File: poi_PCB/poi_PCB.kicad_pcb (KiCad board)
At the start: 2 copper layers, 60 x 60 mm, 73 parts, among them J1 ANALOG_RGB_HEADER, J4 USB_C_Receptacle_USB2.0, Q1 AO4407C, Q2 AO3400A, Q3 AO3400A, Q4 AO3400A, Q5 AO4407C, Q6 AO3400A, Q7 AO3400A, Q8 AO3400A, SW3 TL2233OA, U1 ESP32-WROOM-32D, U2 CH340C, U3 AMS1117-3.3, U4 LSM6DS33TR, U5 LIS2DH, U6 MH-CD42

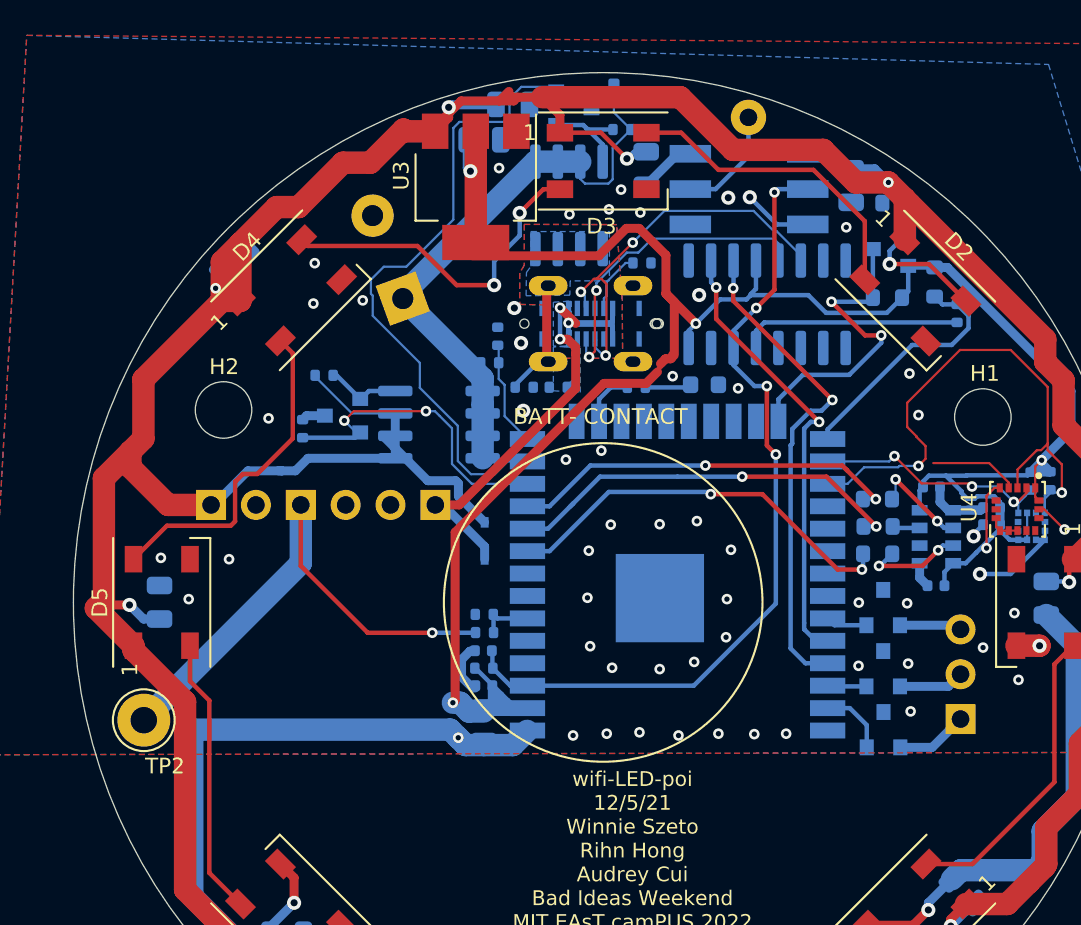
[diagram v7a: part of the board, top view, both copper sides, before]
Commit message: Changed schematic based on testing
-LED logic level shifter omitted due to slow switching speed of AO3400A
-LED input moved to GPIO5 to avoid pulling up GPIO2 during UART programming
-Gate pullup/pulldown resistors changed to 1K to allow for faster switching
-analog RGB header omitted
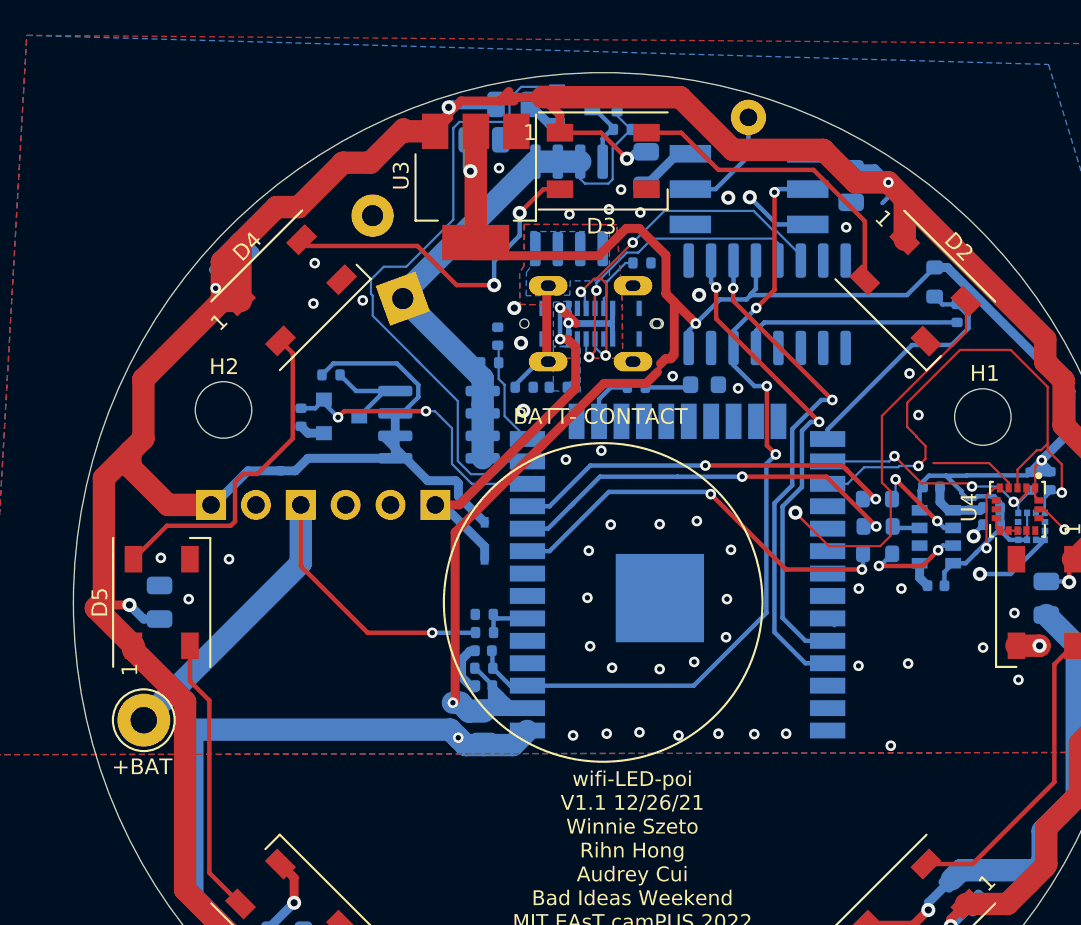
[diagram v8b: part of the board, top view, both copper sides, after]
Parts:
- removed J1: ANALOG_RGB_HEADER, Connector_PinHeader_2.54mm:PinHeader_1x03_P2.54mm_Vertical
- removed Q3, Q4, Q7, Q8: AO3400A, Package_TO_SOT_SMD:SOT-23
- removed R14, R15: 10K, Resistor_SMD:R_0603_1608Metric
- C4: value CP1_Small -> 0.47F
- R11, R13, R17, R18: value 10K -> 1K
- moved Q6 33.2 mm to (105.9, 49.5), turned to 0 degrees
- moved R13 0.65 mm to (90.4, 67.0), turned to 90 degrees
- moved R17 0.62 mm to (108.3, 49.2)
- moved R11 0.39 mm to (92.1, 64.6)
- moved Q2 0.07 mm to (92.7, 67.0), turned to 0 degrees
- renumbered TP2 to +BAT, TP1 to EN_L
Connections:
- D2 pad 4: /LED_SIG_5 -> /LED_SIG
- Q2 pad 1: Net-(Q1-Pad4) -> GND
- Q2 pad 3: GND -> Net-(Q1-Pad4)
- Q5 pad 4: Net-(Q4-Pad1) -> Net-(Q5-Pad4)
- Q6 pad 1: Net-(J1-Pad3) -> GND
- Q6 pad 2: /RED -> /FIRE_L
- Q6 pad 3: GND -> Net-(Q5-Pad4)
- R18 pad 2: Net-(Q4-Pad1) -> Net-(Q5-Pad4)
- U1 pad 24: /LED_SIG_3.3 -> (no net)
- U1 pad 29: (no net) -> /LED_SIG
- U1 pad 33: /RED -> (no net)
- U1 pad 36: /GREEN -> (no net)
- U1 pad 37: /BLUE -> (no net)
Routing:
- net /LED_SIG: track 0.00 -> 24.1 mm, vias 0 -> 1
- net /LED_SIG_3.3: track 17.6 -> 0.00 mm, vias 2 -> 0
- net /LED_SIG_5: track 9.10 -> 0.00 mm, vias 1 -> 0
- net Net-(Q4-Pad1): track 5.94 -> 0.00 mm
- net Net-(Q5-Pad4): track 0.00 -> 4.26 mm
- net Net-(J1-Pad3): track 4.12 -> 0.00 mm
- net Net-(J1-Pad1): track 4.07 -> 0.00 mm
- net /BLUE: track 3.87 -> 0.00 mm
- net Net-(J1-Pad2): track 3.71 -> 0.00 mm
- net +5V: track 247.9 -> 250.9 mm
- net /RED: track 2.36 -> 0.00 mm
- net /GREEN: track 2.21 -> 0.00 mm
- net Net-(Q1-Pad4): track 4.26 -> 6.14 mm
- net +3V3: track 138.0 -> 136.2 mm
- net GND: track 132.6 -> 131.0 mm, vias 60 -> 59
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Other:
- board text added: "wifi-LED-poi V1.1 12/26/21 Winnie Szeto Rihn Hong Audrey Cui Bad Ideas Weekend MIT EAsT camPUS 2022 github.com/wszeto9/wifi-LED-poi"
- board text removed: "wifi-LED-poi 12/5/21 Winnie Szeto Rihn Hong Audrey Cui Bad Ideas Weekend MIT EAsT camPUS 2022 github.com/wszeto9/wifi-LED-poi"
